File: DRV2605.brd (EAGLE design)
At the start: 50 x 13.5 mm, 49 parts, among them U1 DRV2605L, U2 DRV2605L, U3 DRV2605L, U4 DRV2605L, U5 DRV2605L, U6 DRV2605L, U7 DRV2605L

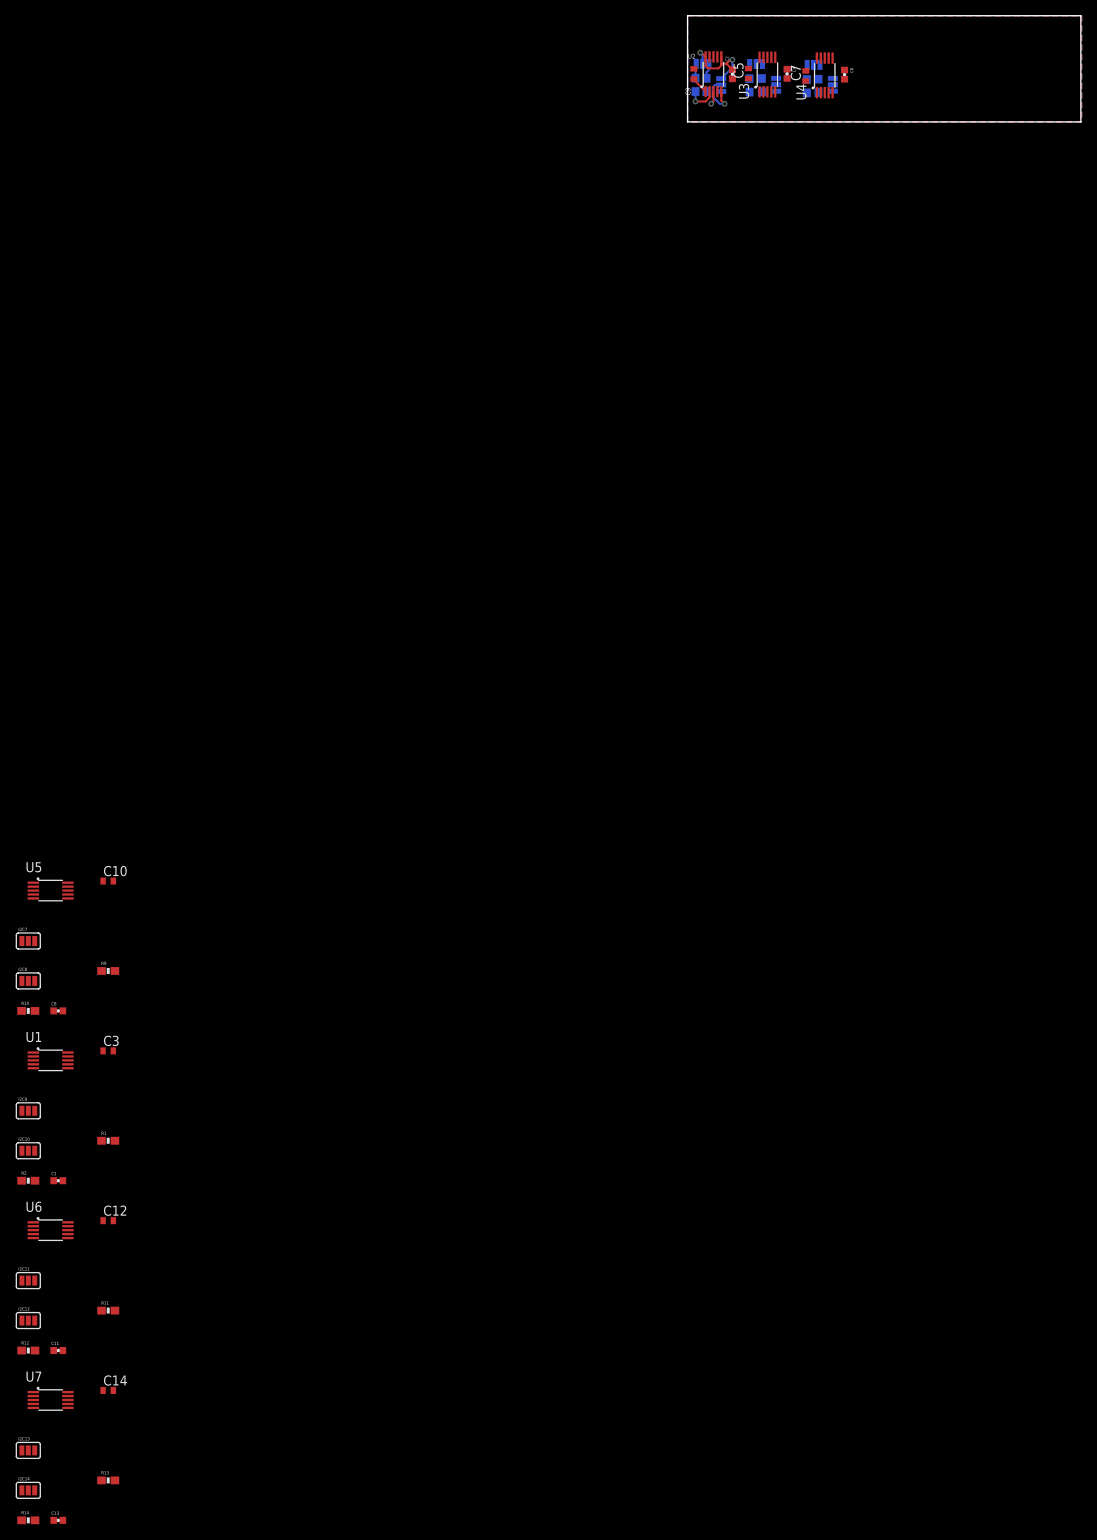
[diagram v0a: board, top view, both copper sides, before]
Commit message: DRV routing done
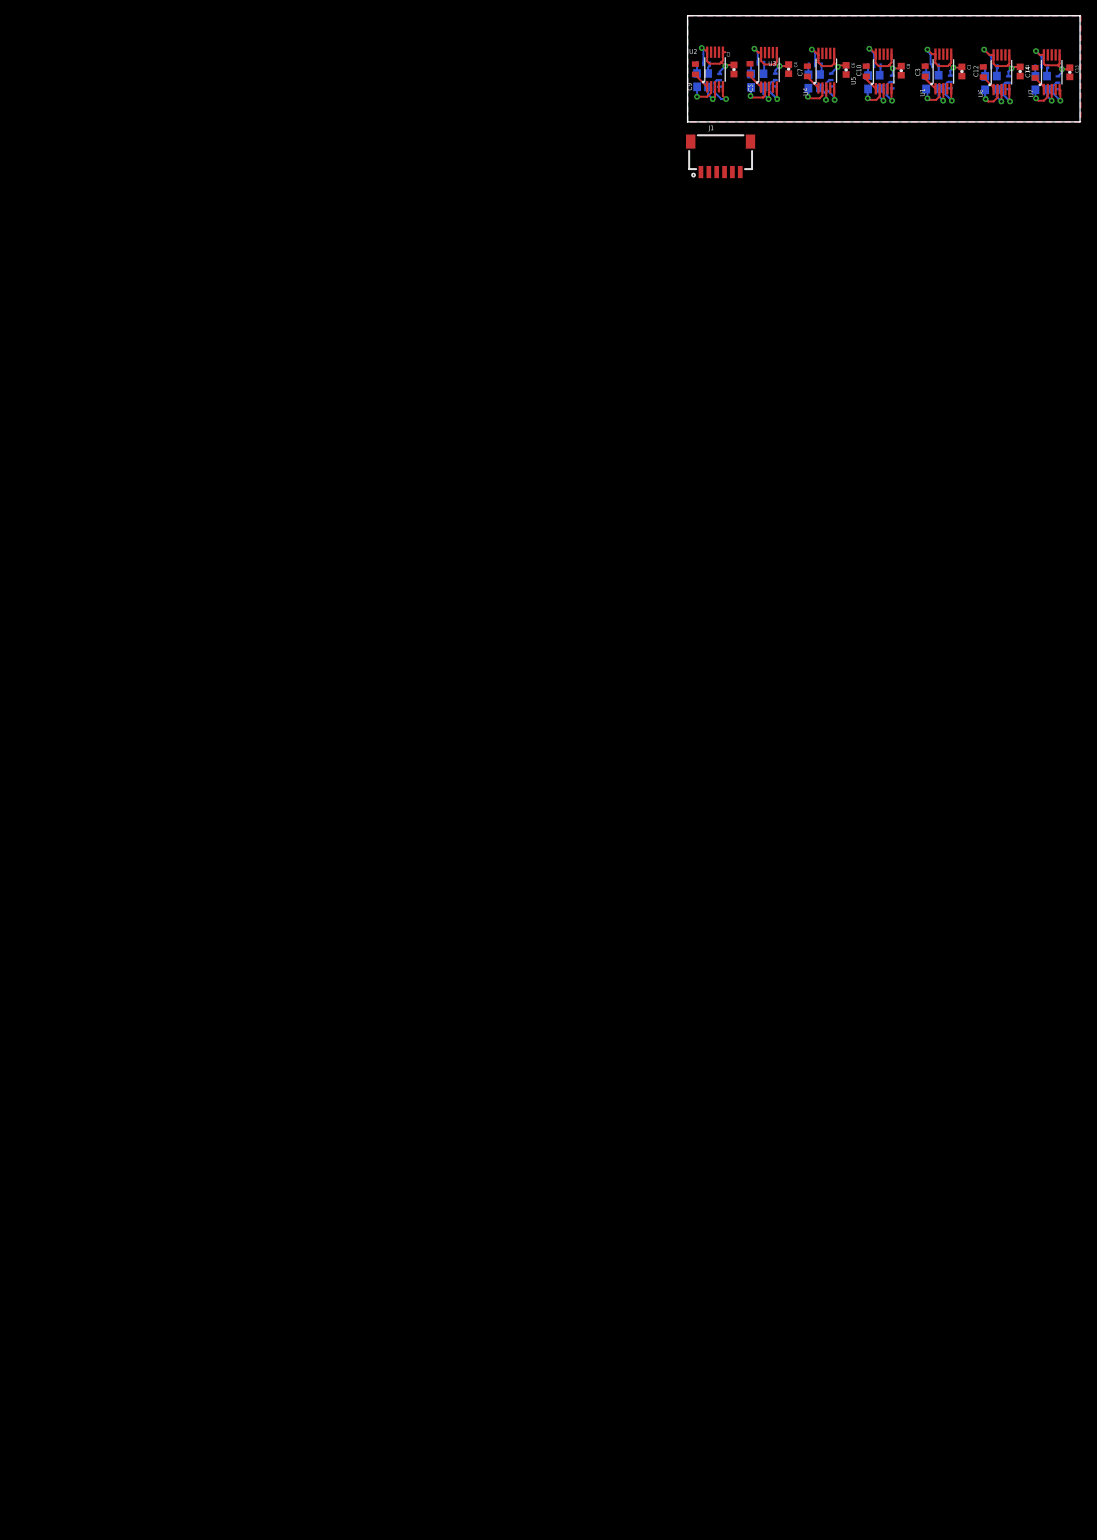
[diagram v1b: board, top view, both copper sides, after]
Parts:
- added J1: BM06B-SRSS-TB, SparkFun-Connectors:JST-6-SMD-HORI-1.0MM
- I2C1, I2C10, I2C11, I2C12, I2C13, I2C14, I2C2, I2C3, I2C4, I2C5, I2C6, I2C7, I2C8, I2C9: value JUMPER-PAD-3-NC_BY_PASTE -> JUMPER_3PLACE_NO_XTRA_SMALL; device SparkFun-Passives:PAD-JUMPER-3-NC_BY_PASTE_YES_SILK_FULL_BOX -> yhtomit_jumpers:XTRA_SMALL_JUMPER_3_NO
- moved C13 224.6 mm to (48.6, 6.31), turned to 270 degrees
- moved R14 224.0 mm to (45.7, 4.98), flipped to the bottom, turned to 90 degrees
- moved I2C14 221.7 mm to (47.1, 4.98), flipped to the bottom, turned to 270 degrees
- moved I2C13 218.1 mm to (45.0, 7.01), flipped to the bottom, turned to 180 degrees
- moved R13 213.2 mm to (44.2, 4.94), flipped to the bottom, turned to 90 degrees
- moved U7 211.5 mm to (46.4, 6.02), turned to 90 degrees
- moved C14 204.8 mm to (44.2, 6.24), turned to 90 degrees
- moved C11 203.5 mm to (42.3, 6.41), turned to 270 degrees
- moved R12 202.8 mm to (39.3, 4.98), flipped to the bottom, turned to 90 degrees
- moved I2C12 200.7 mm to (40.8, 4.98), flipped to the bottom, turned to 270 degrees
- moved I2C11 197.0 mm to (38.6, 7.02), flipped to the bottom, turned to 180 degrees
- moved R11 191.8 mm to (37.8, 4.94), flipped to the bottom, turned to 90 degrees
- moved U6 190.5 mm to (40.0, 6.02), turned to 90 degrees
- moved C12 183.6 mm to (37.6, 6.34), turned to 90 degrees
- moved C1 181.9 mm to (34.9, 6.41), turned to 270 degrees
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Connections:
- new net N$22: J1.1
- new net N$23: J1.2
- new net N$24: J1.3
- new net N$25: J1.4
- new net N$26: J1.5
- new net N$27: J1.6
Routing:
- net VCC: track 12.7 -> 77.2 mm, vias 2 -> 14
- net EN3: track 0.00 -> 4.92 mm, vias 0 -> 1
- net EN6: track 0.00 -> 4.84 mm, vias 0 -> 1
- net EN2: track 0.00 -> 4.84 mm, vias 0 -> 1
- net EN4: track 0.00 -> 4.71 mm, vias 0 -> 1
- net EN5: track 0.00 -> 4.71 mm, vias 0 -> 1
- net EN7: track 0.00 -> 4.48 mm, vias 0 -> 1
- net SCL2: track 0.00 -> 4.22 mm, vias 0 -> 1
- net SCL3: track 0.00 -> 4.15 mm, vias 0 -> 1
- net SCL6: track 0.00 -> 4.07 mm, vias 0 -> 1
- net SCL5: track 0.00 -> 4.03 mm, vias 0 -> 1
- net SCL4: track 0.00 -> 3.99 mm, vias 0 -> 1
- net SCL7: track 0.00 -> 3.87 mm, vias 0 -> 1
- net SDA3: track 0.00 -> 3.38 mm, vias 0 -> 1
- net SDA2: track 0.00 -> 3.33 mm, vias 0 -> 1
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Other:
- board size 50 x 13.5 mm -> 49.9 x 13.5 mm

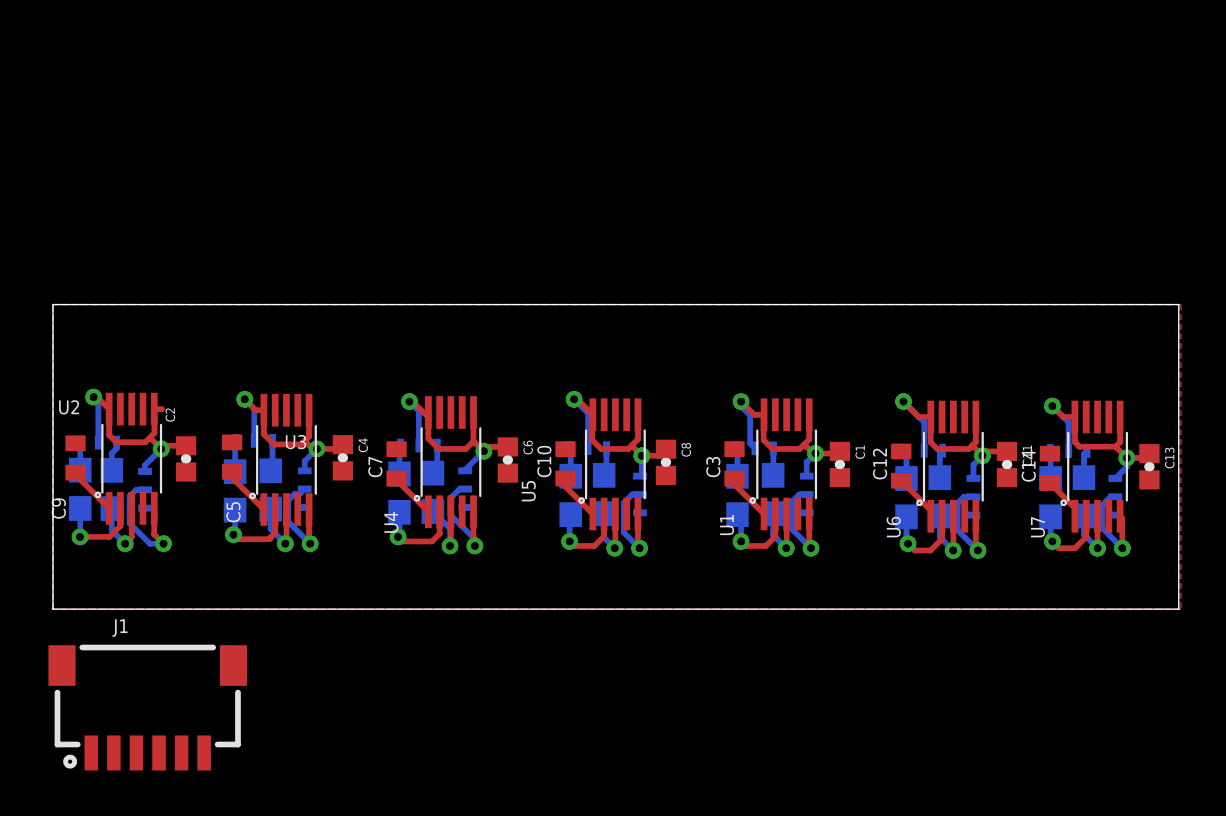
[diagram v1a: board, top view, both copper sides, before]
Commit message: TCA added and routed to 5 fingers
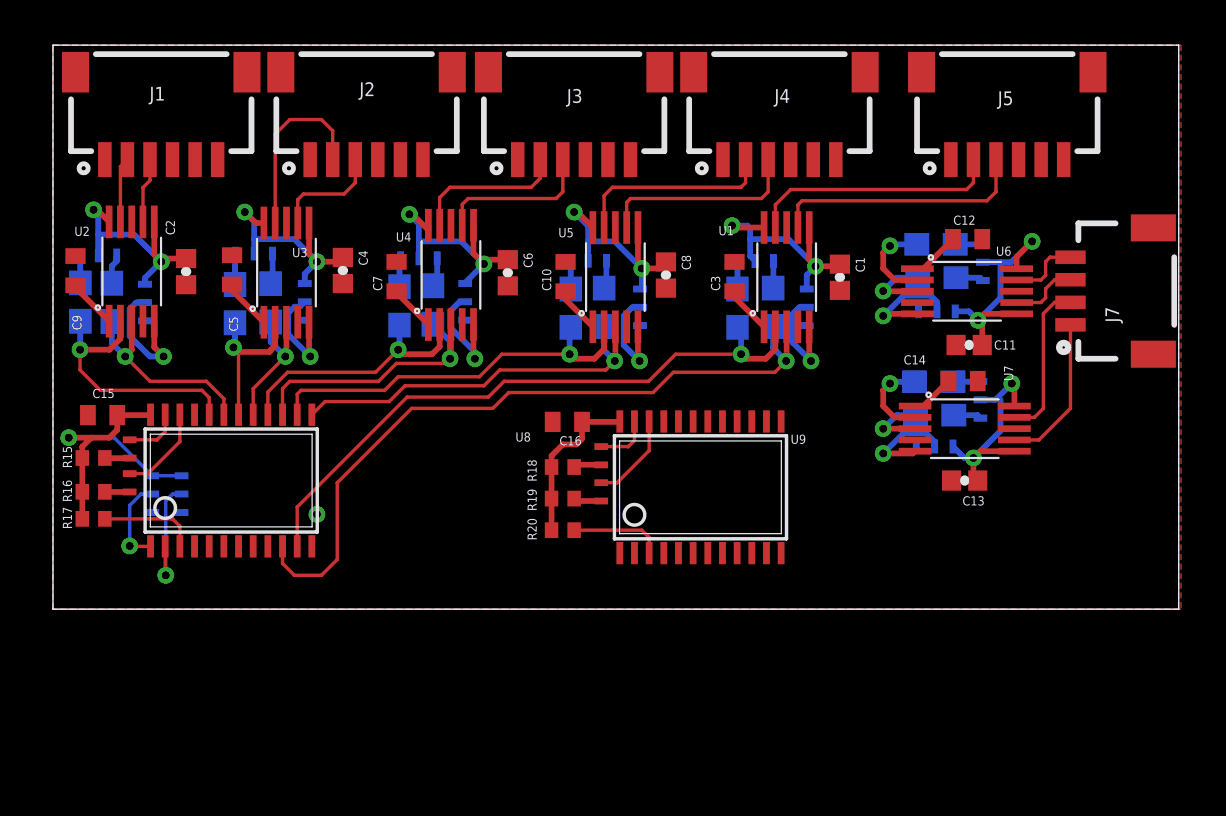
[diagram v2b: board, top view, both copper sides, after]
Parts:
- added C15, C16: 10uF, resistor:C0402
- added J2, J3, J4, J5: BM06B-SRSS-TB, SparkFun-Connectors:JST-6-SMD-HORI-1.0MM
- added J7: (no value), SparkFun-Connectors:1X04_1MM_RA
- added R15, R16, R17, R18, R19, R20: 10K, rcl:R0402
- added SCLPU, SCLPU1, SDAPU, SDAPU1: JUMPER_2PLACE_NO_XTRA_SMALL, yhtomit_jumpers:XTRA_SMALLJUMPER_NO
- added U$5, U$6: JUMPER_3PLACE_NO_XTRA_SMALL, yhtomit_jumpers:XTRA_SMALL_JUMPER_3_NO
- added U8, U9: TCA9548APWR, microbuilder:TSSOP24
- moved J1 26.3 mm to (4.80, 24.7)
- moved R11 11.3 mm to (39.1, 16.2), turned to 180 degrees
- moved C12 10.5 mm to (40.5, 16.4), turned to 0 degrees
- moved R12 9.71 mm to (39.2, 14.7), turned to 180 degrees
- moved I2C11 8.75 mm to (41.2, 15.4), turned to 270 degrees
- moved I2C12 8.38 mm to (39.2, 13.2), turned to 0 degrees
- moved I2C14 8.31 mm to (39.1, 7.21), turned to 0 degrees
- moved C1 8.30 mm to (34.9, 14.7)
- moved C10 8.30 mm to (22.7, 14.7)
- moved C2 8.30 mm to (5.90, 15.0)
- moved C3 8.30 mm to (30.2, 14.7)
- moved C4 8.30 mm to (12.8, 15.0)
- moved C6 8.30 mm to (20.2, 14.9)
- moved C7 8.30 mm to (15.2, 14.7)
- moved C8 8.30 mm to (27.2, 14.8)
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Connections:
- new net 0SCL: U8.5
- new net 0SCL1: U9.5
- new net 0SDA: U8.4
- new net 0SDA1: U9.4
- new net 1SCL: U8.7
- new net 1SCL1: U9.7
- new net 1SDA: U8.6
- new net 1SDA1: U9.6
- new net 2SCL: U8.9
- new net 2SCL1: U9.9
- new net 2SDA: U8.8
- new net 2SDA1: U9.8
- new net 3SCL1: U9.11
- new net 3SDA1: U9.10
- new net 4SCL1: U9.14
- new net 4SDA1: U9.13
- new net 5SCL1: U9.16
- new net 5SDA1: U9.15
- new net 6SCL1: U9.18
- new net 6SDA1: U9.17
- new net 7SCL1: U9.20
- new net 7SDA1: U9.19
- new net INPUTSCL: SCLPU.1, U8.22
- new net INPUTSCL1: SCLPU1.1, U9.22
- new net INPUTSDA: SDAPU.1, U8.23
- new net INPUTSDA1: SDAPU1.1, U9.23
- new net N$28: J2.4
- new net N$29: J2.5
- new net N$30: U$6.2, U8.2
- new net N$32: J3.4
- new net N$33: J3.5
- new net N$36: J4.4
- new net N$37: J4.5
- new net N$40: J5.4
- new net N$41: J5.5
- new net N$42: R19.1, SCLPU1.2
- new net N$43: R18.1, SDAPU1.2
- new net RESET: R17.1, U8.3
- new net RESET1: R20.1, U9.3
- net +OUT1: now also J1.3
- net +OUT2: now also J2.3
- net +OUT3: now also J3.3
- net +OUT4: now also J4.3
- net +OUT5: now also J5.3
- net +OUT6: now also J7.3
- net +OUT7: now also J7.1
- net -OUT1: now also J1.2
- net -OUT2: now also J2.2
- net -OUT3: now also J3.2
- net -OUT4: now also J4.2
- net -OUT5: now also J5.2
- net -OUT6: now also J7.4
- net -OUT7: now also J7.2
- net GND: now also C15.2, C16.2, J1.1, J2.1, J3.1, J4.1, J5.1, U$5.1, U$6.1, U8.12, U9.1, U9.12, U9.2, U9.21
- net N$22: now also U8.21; no longer J1.1
- net N$23: now also R16.1, SCLPU.2; no longer J1.2
- net N$24: now also R15.1, SDAPU.2; no longer J1.3
- net N$27: now also U$5.2, U8.1; no longer J1.6
- net SCL1: now also U8.20
- net SCL2: now also U8.18
- net SCL3: now also U8.16
- net SCL4: now also U8.14
- net SCL5: now also U8.11
- net SDA1: now also U8.19
- net SDA2: now also U8.17
- net SDA3: now also U8.15
- net SDA4: now also U8.13
- net SDA5: now also U8.10
- net VCC: now also C15.1, C16.1, J1.6, J2.6, J3.6, J4.6, J5.6, R15.2, R16.2, R17.2, R18.2, R19.2, R20.2, U$5.3, U$6.3, U8.24, U9.24
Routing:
- net SDA5: track 3.29 -> 32.5 mm
- net SCL5: track 4.03 -> 28.3 mm
- net VCC: track 77.2 -> 96.9 mm, vias 14 -> 15
- net SDA4: track 3.25 -> 17.7 mm
- net SCL4: track 3.99 -> 17.7 mm
- net +OUT5: track 0.00 -> 11.5 mm
- net -OUT5: track 0.00 -> 11.2 mm
- net SDA3: track 3.38 -> 12.5 mm
- net +OUT4: track 0.00 -> 9.00 mm
- net -OUT4: track 0.00 -> 8.95 mm
- net -OUT2: track 0.00 -> 8.24 mm
- net SCL1: track 4.03 -> 11.9 mm
- net SCL3: track 4.15 -> 11.7 mm
- net -OUT7: track 0.00 -> 7.06 mm
- net +OUT3: track 0.00 -> 7.04 mm
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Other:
- board size 49.9 x 13.5 mm -> 49.9 x 25 mm

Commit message: working on control pins
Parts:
- removed I2C1, I2C11, I2C13, I2C3, I2C5, I2C7, I2C9: JUMPER_3PLACE_NO_XTRA_SMALL, yhtomit_jumpers:XTRA_SMALL_JUMPER_3_NO
- removed SCLPU, SCLPU1, SDAPU, SDAPU1: JUMPER_2PLACE_NO_XTRA_SMALL, yhtomit_jumpers:XTRA_SMALLJUMPER_NO
- moved C5 2.40 mm to (7.26, 12.7), turned to 180 degrees
- moved C16 2.18 mm to (20.7, 7.70)
- moved U9 2.18 mm to (26.6, 4.80)
- moved C4 1.59 mm to (12.7, 16.6), turned to 90 degrees
- moved C2 1.58 mm to (5.80, 16.5), turned to 90 degrees
- moved C9 1.41 mm to (1.20, 13.6)
- moved R18 1.24 mm to (21.4, 6.00)
- moved R19 1.22 mm to (21.4, 4.70)
- moved R20 1.20 mm to (21.4, 3.40)
- moved R16 0.95 mm to (2.70, 5.50)
- moved R15 0.92 mm to (2.70, 6.90)
- moved R17 0.92 mm to (2.70, 4.20)
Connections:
- net 2SCL1 renamed IMU_SCL6
- net 2SDA1 renamed IMU_SDA6
- removed net 3SCL1: U9.11
- removed net 3SDA1: U9.10
- removed net 4SCL1: U9.14
- removed net 4SDA1: U9.13
- removed net 5SCL1: U9.16
- removed net 5SDA1: U9.15
- removed net 6SCL1: U9.18
- removed net 6SDA1: U9.17
- removed net 7SCL1: U9.20
- removed net 7SDA1: U9.19
- removed net N$11: I2C1.3, R4.2
- removed net N$12: I2C1.1, R3.2
- removed net N$14: I2C3.3, R6.2
- removed net N$15: I2C3.1, R5.2
- removed net N$17: I2C5.3, R8.2
- removed net N$18: I2C5.1, R7.2
- removed net N$2: I2C9.3, R2.2
- removed net N$20: I2C7.3, R10.2
- removed net N$21: I2C7.1, R9.2
- removed net N$23: R16.1, SCLPU.2
- removed net N$24: R15.1, SDAPU.2
- removed net N$25: J1.4
- removed net N$26: J1.5
- removed net N$28: J2.4
- removed net N$29: J2.5
- removed net N$3: I2C9.1, R1.2
- removed net N$32: J3.4
- removed net N$33: J3.5
- removed net N$36: J4.4
- removed net N$37: J4.5
- removed net N$40: J5.4
- removed net N$41: J5.5
- removed net N$42: R19.1, SCLPU1.2
- removed net N$43: R18.1, SDAPU1.2
- removed net N$5: I2C11.3, R12.2
- removed net N$6: I2C11.1, R11.2
- removed net N$8: I2C13.3, R14.2
- removed net N$9: I2C13.1, R13.2
- new net IMU_SCL1: J1.5, U9.20
- new net IMU_SCL2: J2.5, U9.18
- new net IMU_SCL3: J3.5, U9.16
- new net IMU_SCL4: J4.5, U9.14
- new net IMU_SCL5: J5.5, U9.11
- new net IMU_SDA1: J1.4, U9.19
- new net IMU_SDA2: J2.4, U9.17
- new net IMU_SDA3: J3.4, U9.15
- new net IMU_SDA4: J4.4, U9.13
- new net IMU_SDA5: J5.4, U9.10
- net INPUTSCL: now also R16.1; no longer SCLPU.1
- net INPUTSCL1: now also R19.1; no longer SCLPU1.1
- net INPUTSDA: now also R15.1; no longer SDAPU.1
- net INPUTSDA1: now also R18.1; no longer SDAPU1.1
- net VCC: now also R1.2, R10.2, R11.2, R12.2, R13.2, R14.2, R2.2, R3.2, R4.2, R5.2, R6.2, R7.2, R8.2, R9.2; no longer I2C1.2, I2C11.2, I2C13.2, I2C3.2, I2C5.2, I2C7.2, I2C9.2
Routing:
- net IMU_SDA1: track 0.00 -> 37.3 mm, vias 0 -> 2
- net IMU_SCL1: track 0.00 -> 34.4 mm, vias 0 -> 2
- net IMU_SCL5: track 0.00 -> 29.4 mm, vias 0 -> 2
- net IMU_SDA5: track 0.00 -> 29.2 mm, vias 0 -> 2
- net IMU_SDA2: track 0.00 -> 26.6 mm, vias 0 -> 2
- net IMU_SCL2: track 0.00 -> 23.2 mm, vias 0 -> 2
- net IMU_SDA3: track 0.00 -> 22.3 mm, vias 0 -> 2
- net IMU_SDA4: track 0.00 -> 21.9 mm, vias 0 -> 2
- net IMU_SCL4: track 0.00 -> 19.4 mm, vias 0 -> 2
- net IMU_SCL3: track 0.00 -> 18.3 mm, vias 0 -> 2
- net VCC: track 96.9 -> 109.5 mm
- net N$13: track 2.26 -> 0.00 mm
- net N$15: track 1.39 -> 0.00 mm
- net N$14: track 1.36 -> 0.00 mm
- net N$11: track 1.32 -> 0.00 mm
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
